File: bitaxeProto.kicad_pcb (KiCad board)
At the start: 6 copper layers, 76 x 101 mm, 207 parts, among them J1 XT30, J4 Conn_01x04, J5 Conn_01x10, J6 USB_C_Receptacle_USB2.0, J8 TC2030-IDC, Q1 BSS138, SW3 SWITCH-SPST, SW4 SWITCH-SPST, U1 STHW4-DU-HN050206, U12 ESP32-S3-WROOM-1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

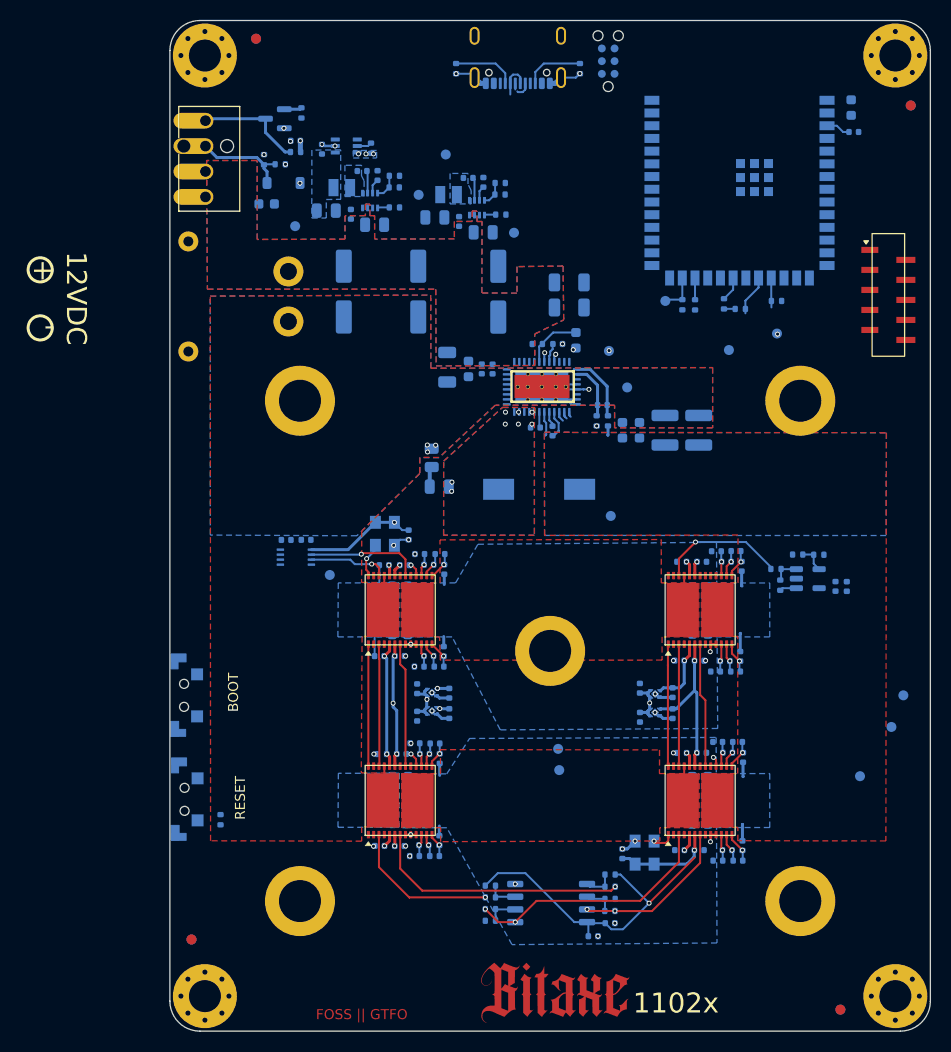
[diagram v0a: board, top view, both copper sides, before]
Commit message: remove old bzm2 stuff
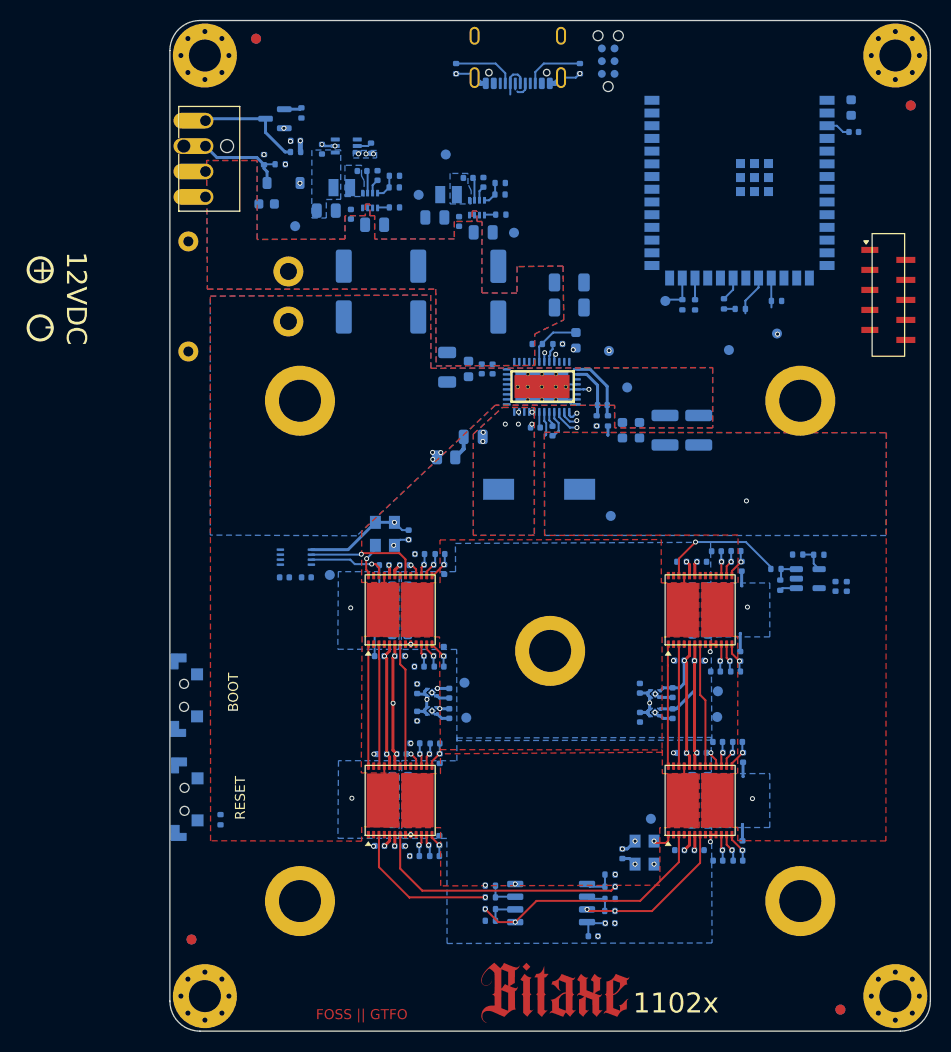
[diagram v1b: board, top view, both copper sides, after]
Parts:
- moved TP11 21.3 mm to (141.1, 128.8)
- moved TP2 18.5 mm to (147.8, 116.0), turned to 0 degrees
- moved TP4 17.4 mm to (147.7, 118.6), turned to 0 degrees
- moved TP6 11.5 mm to (122.4, 115.2), turned to 0 degrees
- moved TP12 10.7 mm to (122.6, 118.7), turned to 0 degrees
- moved C17 6.02 mm to (123.3, 90.6)
- moved C59 3.75 mm to (106.6, 104.7)
- moved C61 3.74 mm to (104.5, 104.7)
- moved R6 1.44 mm to (120.6, 92.7), turned to 180 degrees
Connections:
- C59 pad 2: Net-(U14-GND) -> GND
- C61 pad 2: Net-(U14-GND) -> GND
- U14 pad 4: Net-(U14-GND) -> GND
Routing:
- net /5V_SWITCH: track 123.5 -> 147.7 mm
- net /ASIC/0V75-0: track 11.5 -> 20.8 mm
- net /ASIC/GND0: track 21.0 -> 17.4 mm
- net /ASIC/1V2-0: track 60.8 -> 62.9 mm, vias 5 -> 9
- net /Data/SCL: track 4.94 -> 6.63 mm, vias 0 -> 1
- net /Data/SDA: track 2.96 -> 4.14 mm, vias 1 -> 2
- net /Power/PGOOD: track 4.62 -> 5.39 mm, vias 0 -> 1
- net GND: vias 33 -> 36
- net /VDD: vias 0 -> 3

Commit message: lots of signal routing
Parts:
- moved R22 93.5 mm to (161.3, 60.0), turned to 0 degrees
- moved C209 24.4 mm to (164.4, 81.4), turned to 0 degrees
- moved C208 23.5 mm to (164.4, 82.6), turned to 0 degrees
- moved R25 20.8 mm to (166.1, 84.3), turned to 90 degrees
- moved U13 20.6 mm to (163.6, 85.3), turned to 90 degrees
- moved R70 20.1 mm to (164.2, 88.1), turned to 0 degrees
- moved R26 18.0 mm to (166.1, 86.4), turned to 90 degrees
- moved R71 17.8 mm to (162.6, 88.5), turned to 90 degrees
- moved C59 14.7 mm to (120.8, 100.9)
- moved C61 14.7 mm to (118.6, 100.9)
- moved U14 14.7 mm to (119.8, 98.9)
- moved TP13 12.8 mm to (107.9, 63.9)
- moved TP10 3.60 mm to (112.4, 103.2)
- moved C48 1.07 mm to (161.3, 61.2)
- moved C16 0.14 mm to (129.4, 89.7)
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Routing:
- net /3V3: track 1.22 -> 133.7 mm, vias 1 -> 15
- net /Data/EN: track 2.45 -> 109.8 mm, vias 0 -> 4
- net /Data/IO0: track 0.00 -> 79.4 mm, vias 0 -> 2
- net /ASIC/RX_3V3: track 0.00 -> 65.7 mm, vias 0 -> 2
- net /Data/ASIC_RST: track 0.00 -> 50.9 mm, vias 0 -> 2
- net /Data/USB_D+: track 2.16 -> 42.0 mm, vias 0 -> 2
- net /Data/USB_D-: track 3.57 -> 42.5 mm, vias 0 -> 2
- net /12V: track 0.00 -> 37.7 mm
- net /Data/SMB_ALRT: track 4.99 -> 29.7 mm, vias 0 -> 2
- net /Data/PWR_EN: track 5.16 -> 29.3 mm, vias 1 -> 2
- net /ASIC/TX_3V3: track 1.70 -> 25.8 mm, vias 0 -> 2
- net /Power/PGOOD: track 5.39 -> 26.4 mm, vias 1 -> 2
- net /Data/SCL: track 6.63 -> 25.5 mm, vias 1 -> 2
- net /Data/SDA: track 4.14 -> 22.4 mm, vias 2 -> 3
- net /ASIC/TX_2V4: track 12.8 -> 27.0 mm, vias 1 -> 2
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- added copper zone on B.Cu, net /3V3
- removed copper zone on In2.Cu, net /12V
- removed copper zone on In2.Cu, net /Power/SW1

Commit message: lots of DRC fixes. adding power plane via grid.
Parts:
- removed TP20, TP27: GND, bitaxe:TestPoint_Pad_D1.0mm
- C1, C2, C3: footprint Capacitor_SMD:C_Elec_6.3x7.7 -> Capacitor_SMD:C_Elec_5x5.4
- moved C19 8.46 mm to (139.0, 81.0), turned to -90 degrees
- moved TP5 7.06 mm to (143.7, 80.1)
- moved TP11 6.00 mm to (136.5, 132.7)
- moved TP1 5.39 mm to (153.1, 78.6)
- moved C6 4.92 mm to (136.5, 81.0), turned to -90 degrees
- moved C3 3.87 mm to (122.2, 77.5), turned to 180 degrees
- moved C2 2.40 mm to (115.4, 76.2)
- moved TP12 1.73 mm to (121.9, 120.3)
- moved TP6 0.96 mm to (121.9, 114.4)
- moved C1 0.90 mm to (109.5, 76.1)
- moved TP21 0.43 mm to (105.9, 69.3)
- moved SW4 0.27 mm to (96.6, 116.4)
- moved SW3 0.27 mm to (96.6, 126.8)
- moved TP4 0.07 mm to (147.8, 118.6)
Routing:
- net /Data/FAN_TACH: track 0.00 -> 61.8 mm, vias 1 -> 2
- net /Data/FAN_PWM: track 0.01 -> 60.6 mm, vias 0 -> 2
- net /3V3: track 133.7 -> 165.7 mm, vias 15 -> 16
- net /Data/EN: track 109.8 -> 141.3 mm
- net /Data/IO0: track 79.4 -> 106.4 mm, vias 2 -> 4
- net /Data/DISP_SCL: track 0.00 -> 22.5 mm, vias 0 -> 1
- net /Data/DISP_GPIO1: track 0.00 -> 21.2 mm, vias 0 -> 1
- net /Data/DISP_GPIO2: track 0.00 -> 19.6 mm, vias 0 -> 1
- net /ASIC/1V2-0: track 62.9 -> 81.7 mm, vias 9 -> 13
- net /Data/DISP_SDA: track 0.00 -> 17.7 mm, vias 0 -> 1
- net /Data/P_RX: track 0.00 -> 14.6 mm
- net /Data/P_TX: track 0.00 -> 11.9 mm
- net /VDD: track 7.35 -> 0.92 mm, vias 3 -> 309
- net /ASIC/CLKI-0: track 2.18 -> 8.22 mm, vias 1 -> 2
- net /ASIC/0V75-0: track 20.8 -> 25.5 mm, vias 4 -> 5
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
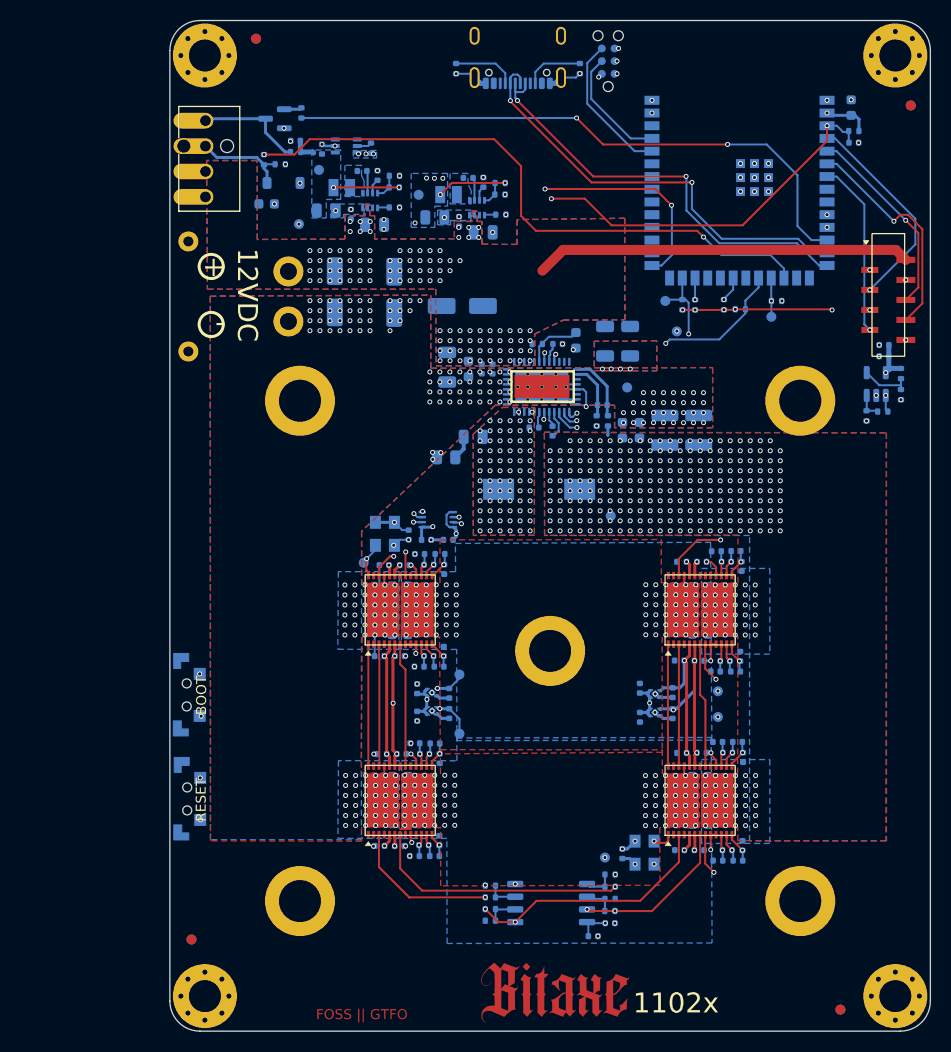
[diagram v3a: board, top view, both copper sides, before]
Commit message: add more data test points. Fix ERC & DRC issues
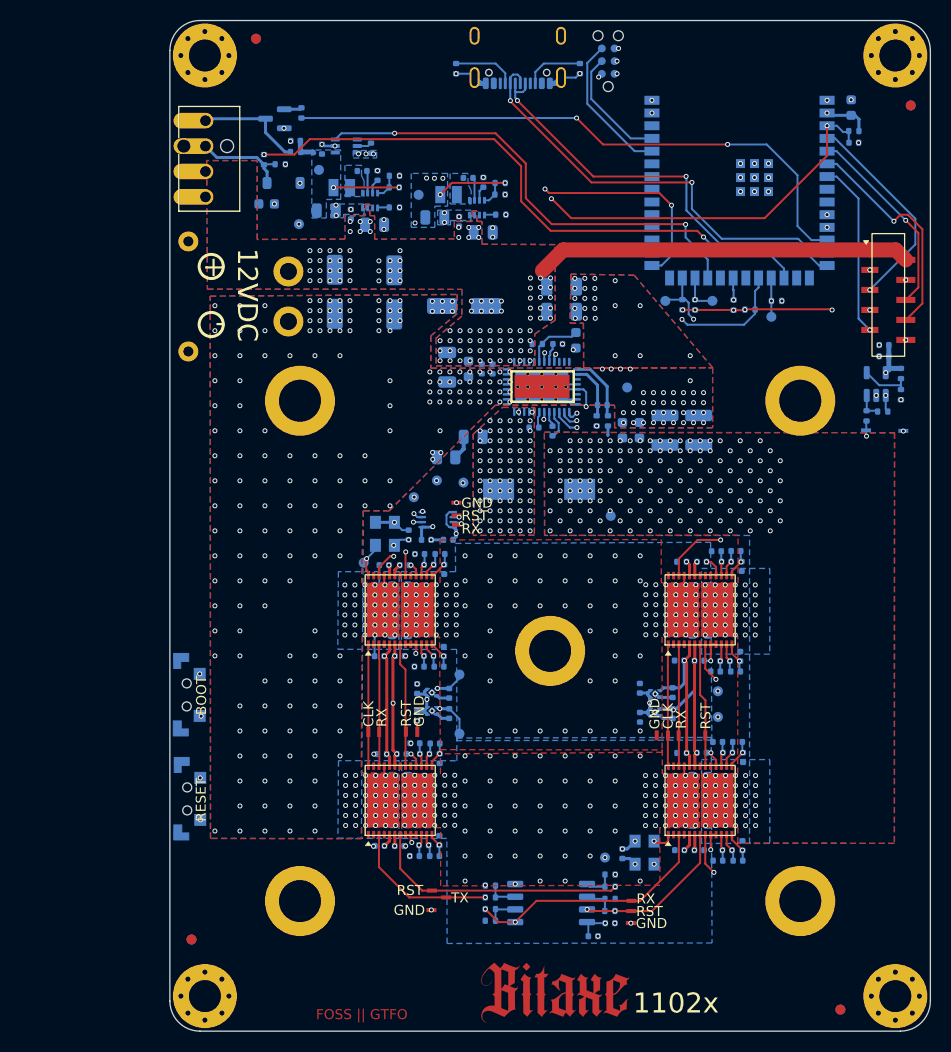
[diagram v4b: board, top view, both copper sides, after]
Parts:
- added TP14: RST, bitaxe:TestPoint_Pad_D1.0mm, B.Cu at (117.4, 96.6)
- added TP15: RX, bitaxe:TestPoint_Pad_D1.0mm, B.Cu at (119.7, 95.0)
- added TP16: GND, bitaxe:TestPoint_Pad_D1.0mm, B.Cu at (122.3, 95.2)
- added TP41: RST, bitaxe:TestPoint_Pad_1.0x0.4mm, F.Cu at (119.2, 135.9)
- added TP42: TX, bitaxe:TestPoint_Pad_1.0x0.4mm, F.Cu at (120.6, 136.6)
- added TP43: RX, bitaxe:TestPoint_Pad_1.0x0.4mm, F.Cu at (139.1, 137.0)
- added TP44: RST, bitaxe:TestPoint_Pad_1.0x0.4mm, F.Cu at (139.1, 138.0)
- added TP45: RX, bitaxe:TestPoint_Pad_1.0x0.4mm, F.Cu at (143.8, 120.4)
- added TP46: CLK, bitaxe:TestPoint_Pad_1.0x0.4mm, F.Cu at (142.8, 120.5)
- added TP47: RX, bitaxe:TestPoint_Pad_1.0x0.4mm, F.Cu at (113.9, 120.1)
- added TP48: CLK, bitaxe:TestPoint_Pad_1.0x0.4mm, F.Cu at (112.8, 120.1)
- added TP49: TX, bitaxe:TestPoint_Pad_1.0x0.4mm, B.Cu at (162.6, 90.0)
- added TP50: RX, bitaxe:TestPoint_Pad_1.0x0.4mm, F.Cu at (121.7, 99.4)
- added TP51: RST, bitaxe:TestPoint_Pad_1.0x0.4mm, F.Cu at (121.7, 98.5)
- added TP52: GND, bitaxe:TestPoint_Pad_1.0x0.4mm, F.Cu at (141.7, 120.4)
- added TP53: GND, bitaxe:TestPoint_Pad_1.0x0.4mm, F.Cu at (117.7, 120.1)
- added TP54: GND, bitaxe:TestPoint_Pad_1.0x0.4mm, F.Cu at (119.1, 137.9)
- added TP55: GND, bitaxe:TestPoint_Pad_1.0x0.4mm, F.Cu at (139.1, 139.2)
- added TP56: RST, bitaxe:TestPoint_Pad_1.0x0.4mm, F.Cu at (146.5, 120.4)
- added TP57: RST, bitaxe:TestPoint_Pad_1.0x0.4mm, F.Cu at (116.6, 120.1)
- added TP58: GND, bitaxe:TestPoint_Pad_1.0x0.4mm, B.Cu at (166.3, 90.0)
- added TP59: GND, bitaxe:TestPoint_Pad_1.0x0.4mm, F.Cu at (121.6, 97.2)
- C1, C2, C3: footprint Capacitor_SMD:C_Elec_5x5.4 -> Capacitor_SMD:CP_Elec_5x5.8
- moved C19 8.76 mm to (132.1, 75.6), turned to 0 degrees
- moved C6 5.25 mm to (132.1, 78.1), turned to 0 degrees
- moved TP5 4.69 mm to (147.2, 77.0)
- moved R20 0.97 mm to (149.3, 77.4)
- moved R21 0.97 mm to (151.0, 77.9)
- moved C3 0.17 mm to (122.4, 77.5)
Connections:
- U12 pad 23: unconnected-(U12-GPIO21-Pad23) -> /Data/5V_EN
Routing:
- net /Data/5V_EN: track 0.00 -> 47.3 mm, vias 0 -> 2
- net /5V_SWITCH: track 150.5 -> 114.3 mm
- net /ASIC/RX_3V3: track 66.9 -> 70.5 mm, vias 2 -> 3
- net /Data/IO0: track 106.4 -> 110.0 mm
- net /Data/EN: track 141.3 -> 144.3 mm
- net /Data/ASIC_RST: track 52.0 -> 54.8 mm, vias 2 -> 3
- net /Data/SDA: track 22.5 -> 24.3 mm, vias 3 -> 2
- net /3V3: track 165.7 -> 167.4 mm
- net /Power/PGOOD: track 26.5 -> 28.0 mm
- net GND: track 46.7 -> 47.9 mm, vias 258 -> 393
- net /Data/FAN_TACH: track 61.8 -> 61.0 mm
- net /ASIC/GND0: vias 152 -> 232
- net /VDD: vias 309 -> 218
- net /12V: vias 106 -> 102
- added copper zone on In1.Cu, net /Power/SW1
- added copper zone on In2.Cu, net /Power/SW1
- added copper zone on In4.Cu, net /Power/SW1
- added copper zone on In2.Cu, net /VDD
